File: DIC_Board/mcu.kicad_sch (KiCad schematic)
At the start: 67 parts, among them J1 DM3AT-SF-PEJM5, J2 Conn_ARM_JTAG_SWD_10, P1 USB_C_Plug_USB2.0, SW1 SW_Push, U1 STM32L476ZGTx, U2 AB-RTCMC-32.768kHz-EOA9-S3, U3 APS6404L-3SQRX-SN, Y1 ABM8AAIG-8.000MHz-V2R-T3, Y2 ABS06-107-32.768KHZ-T

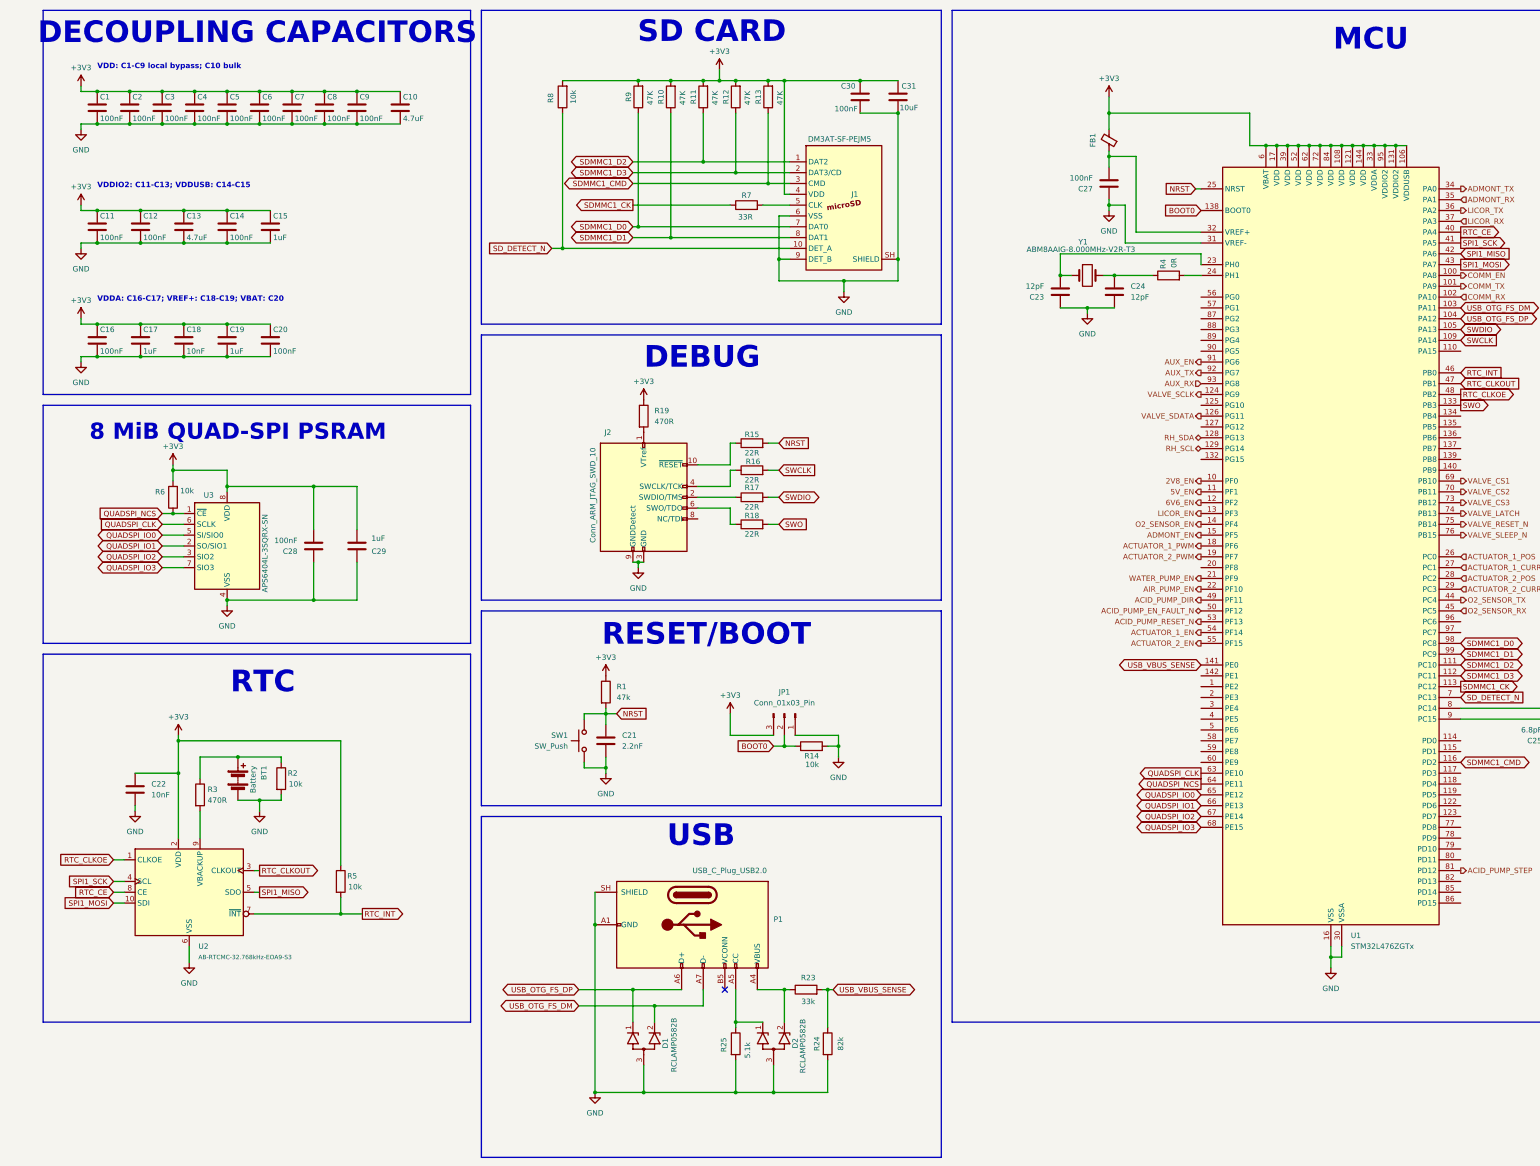
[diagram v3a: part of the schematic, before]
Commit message: Updated board for layout! All footprints added
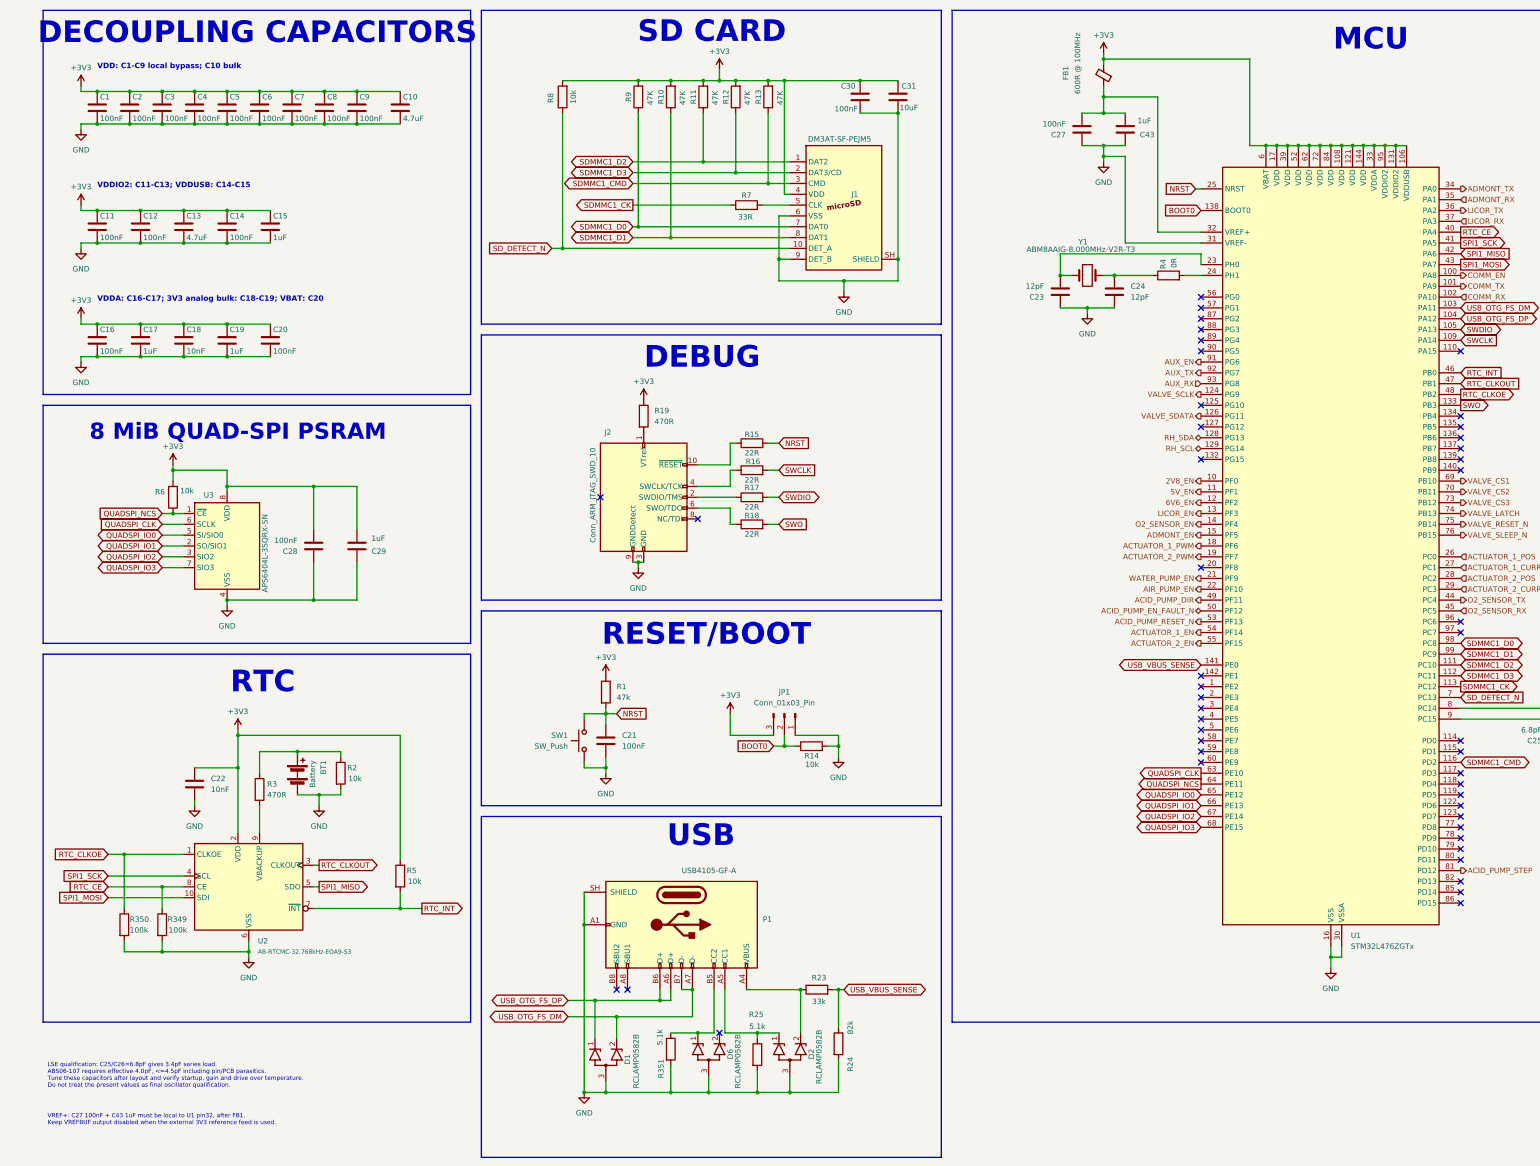
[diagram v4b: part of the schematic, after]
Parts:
- added C43: 1uF, Capacitor_SMD:C_0603_1608Metric, symbol Device:C
- added D6: RCLAMP0582B, Package_TO_SOT_SMD:SOT-523, symbol DIC_Board:RCLAMP0582B_ReviewFixed
- added R349, R350: 100k, Resistor_SMD:R_0603_1608Metric, symbol Device:R
- added R351: 5.1k, Resistor_SMD:R_0402_1005Metric, symbol Device:R
- BT1: footprint (none) -> DIC_Board:BatteryHolder_Keystone_3013_1x16mm; BOM Comments (none) -> 16mm coin-cell retainer only; battery purchased separately.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; BOM Source (none) -> https://www.digikey.com/en/products/detail/keystone-electro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; DigiKey (none) -> 36-3013-ND; MPN (none) -> 3013; Manufacturer (none) -> Keystone Electronics
- C1, C11, C12, C14, C16, C2, C20, C28, C3, C30, C4, C5, C6, C7, C8, C9: BOM Source (none) -> https://product.tdk.com/en/search/capacitor/ceramic/mlcc/in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; Dielectric (none) -> X7R; MPN (none) -> C1608X7R1H104K080AA; Manufacturer (none) -> TDK; Tolerance (none) -> 10%; Voltage Rating (none) -> 50V
- C10, C13: BOM Source (none) -> https://product.tdk.com/en/search/capacitor/ceramic/mlcc/in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; Dielectric (none) -> X7R; MPN (none) -> C2012X7R1E475K125AB; Manufacturer (none) -> TDK; Tolerance (none) -> 10%; Voltage Rating (none) -> 25V
- C15, C17, C19, C29: BOM Source (none) -> https://product.tdk.com/en/search/capacitor/ceramic/mlcc/in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; Dielectric (none) -> X7R; MPN (none) -> C1608X7R1E105K080AB; Manufacturer (none) -> TDK; Tolerance (none) -> 10%; Voltage Rating (none) -> 25V
- C18: BOM Source (none) -> https://product.tdk.com/en/search/capacitor/ceramic/mlcc/in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; Dielectric (none) -> X7R; MPN (none) -> C1608X7R1H103K080AA; Manufacturer (none) -> TDK; Tolerance (none) -> 10%; Voltage Rating (none) -> 50V
- C21: value 2.2nF -> 100nF; footprint (none) -> Capacitor_SMD:C_0603_1608Metric; BOM Source (none) -> https://product.tdk.com/en/search/capacitor/ceramic/mlcc/in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; Dielectric (none) -> X7R; MPN (none) -> C1608X7R1H104K080AA; Manufacturer (none) -> TDK; Tolerance (none) -> 10%; Voltage Rating (none) -> 50V
- C22: footprint (none) -> Capacitor_SMD:C_0603_1608Metric; BOM Source (none) -> https://product.tdk.com/en/search/capacitor/ceramic/mlcc/in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; Dielectric (none) -> X7R; MPN (none) -> C1608X7R1H103K080AA; Manufacturer (none) -> TDK; Tolerance (none) -> 10%; Voltage Rating (none) -> 50V
- C23, C24: footprint (none) -> Capacitor_SMD:C_0603_1608Metric; BOM Source (none) -> https://product.tdk.com/en/search/capacitor/ceramic/mlcc/in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; Dielectric (none) -> C0G; MPN (none) -> C1608C0G1H120J080AA; Manufacturer (none) -> TDK; Tolerance (none) -> 5%; Voltage Rating (none) -> 50V
- C25, C26: footprint (none) -> Capacitor_SMD:C_0402_1005Metric; BOM Source (none) -> https://www.ti.com/lit/df/tidrgo6/tidrgo6.pdf; Dielectric (none) -> C0G; MPN (none) -> GRM1555C1H6R8CA01D; Manufacturer (none) -> Murata; Tolerance (none) -> 0.25pF; Voltage Rating (none) -> 50V
- C27: footprint (none) -> Capacitor_SMD:C_0603_1608Metric; BOM Source (none) -> https://product.tdk.com/en/search/capacitor/ceramic/mlcc/in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; Dielectric (none) -> X7R; MPN (none) -> C1608X7R1H104K080AA; Manufacturer (none) -> TDK; Tolerance (none) -> 10%; Voltage Rating (none) -> 50V
- C31: BOM Source (none) -> https://product.tdk.com/en/search/capacitor/ceramic/mlcc/in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; Dielectric (none) -> X7S; MPN (none) -> C2012X7S1C106K125AC; Manufacturer (none) -> TDK; Tolerance (none) -> 10%; Voltage Rating (none) -> 16V
- D1, D2: symbol Power_Protection:RCLAMP0582B -> DIC_Board:RCLAMP0582B_ReviewFixed
- FB1: value (none) -> 600R @ 100MHz; footprint (none) -> Inductor_SMD:L_0603_1608Metric; BOM Source (none) -> https://www.murata.com/en-us/api/pdfdownloadapi?cate=cgsubC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; Current Rating (none) -> 500mA; DCR Max (none) -> 0.38R; MPN (none) -> BLM18AG601SN1D; Manufacturer (none) -> Murata
- J1: symbol Connector:Micro_SD_Card_Det_Hirose_DM3AT -> DIC_Board:DM3AT_SF_PEJM5_ReviewFixed
- J2: footprint (none) -> DIC_Board:Wurth_61201021621_2x05_P2.54mm_Vertical; BOM Comments (none) -> User-selected 2.54mm-pitch shrouded 10-pin header; retains 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; BOM Source (none) -> https://www.digikey.com/en/products/detail/w%C3%BCrth-elekt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; DigiKey (none) -> 732-2094-ND; MPN (none) -> 61201021621; Manufacturer (none) -> Wurth Elektronik
- JP1: footprint (none) -> DIC_Board:PinHeader_Wurth_61300311121_1x03_P2.54mm_Vertical; BOM Comments (none) -> User specified PTH male header; selected 1x3,2.54mm pitch,v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; BOM Source (none) -> https://www.we-online.com/components/products/datasheet/613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; MPN (none) -> 61300311121; Manufacturer (none) -> Wurth Elektronik
- P1: value USB_C_Plug_USB2.0 -> USB4105-GF-A; footprint (none) -> Connector_USB:USB_C_Receptacle_GCT_USB4105-xx-A_16P_TopMnt_Horizontal; symbol Connector:USB_C_Plug_USB2.0 -> Connector:USB_C_Receptacle_USB2.0_16P; BOM Comments (none) -> Device/UFP socket: CC1 and CC2 each have an independent5.1k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; BOM Source (none) -> https://www.digikey.com/en/products/detail/gct/USB4105-GF-A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; DigiKey (none) -> 2073-USB4105-GF-ACT-ND; MPN (none) -> USB4105-GF-A; Manufacturer (none) -> GCT
- R1: footprint (none) -> Resistor_SMD:R_0603_1608Metric; BOM Source (none) -> https://www.vishay.com/docs/20035/dcrcwe3.pdf; MPN (none) -> CRCW060347K0FKEA; Manufacturer (none) -> Vishay; Power Rating (none) -> 0.125W; Tolerance (none) -> 1%
- R10, R11, R12, R13, R9: BOM Source (none) -> https://www.vishay.com/docs/20035/dcrcwe3.pdf; MPN (none) -> CRCW060347K0FKEA; Manufacturer (none) -> Vishay; Power Rating (none) -> 0.125W; Tolerance (none) -> 1%
- R14, R2, R5: footprint (none) -> Resistor_SMD:R_0603_1608Metric; BOM Source (none) -> https://www.vishay.com/docs/20035/dcrcwe3.pdf; MPN (none) -> CRCW060310K0FKEA; Manufacturer (none) -> Vishay; Power Rating (none) -> 0.125W; Tolerance (none) -> 1%
- R15, R16, R17, R18: footprint (none) -> Resistor_SMD:R_0603_1608Metric; BOM Source (none) -> https://www.vishay.com/docs/20035/dcrcwe3.pdf; MPN (none) -> CRCW060322R0FKEA; Manufacturer (none) -> Vishay; Power Rating (none) -> 0.125W; Tolerance (none) -> 1%
- R19, R3: footprint (none) -> Resistor_SMD:R_0603_1608Metric; BOM Source (none) -> https://www.vishay.com/docs/20035/dcrcwe3.pdf; MPN (none) -> CRCW0603470RFKEA; Manufacturer (none) -> Vishay; Power Rating (none) -> 0.125W; Tolerance (none) -> 1%
- R23: BOM Source (none) -> https://www.vishay.com/docs/20035/dcrcwe3.pdf; MPN (none) -> CRCW040233K0FKED; Manufacturer (none) -> Vishay; Power Rating (none) -> 0.1W; Tolerance (none) -> 1%
- R24: BOM Source (none) -> https://www.vishay.com/docs/20035/dcrcwe3.pdf; MPN (none) -> CRCW040282K0FKED; Manufacturer (none) -> Vishay; Power Rating (none) -> 0.1W; Tolerance (none) -> 1%
- R25: BOM Source (none) -> https://www.vishay.com/docs/20035/dcrcwe3.pdf; MPN (none) -> CRCW04025K10FKED; Manufacturer (none) -> Vishay; Power Rating (none) -> 0.1W; Tolerance (none) -> 1%
- R4: footprint (none) -> Resistor_SMD:R_0603_1608Metric; BOM Source (none) -> https://www.vishay.com/docs/20035/dcrcwe3.pdf; MPN (none) -> CRCW06030000Z0EA; Manufacturer (none) -> Vishay; Power Rating (none) -> 0.125W; Tolerance (none) -> Jumper
- R6, R8: BOM Source (none) -> https://www.vishay.com/docs/20035/dcrcwe3.pdf; MPN (none) -> CRCW060310K0FKEA; Manufacturer (none) -> Vishay; Power Rating (none) -> 0.125W; Tolerance (none) -> 1%
- R7: BOM Source (none) -> https://www.vishay.com/docs/20035/dcrcwe3.pdf; MPN (none) -> CRCW060333R0FKEA; Manufacturer (none) -> Vishay; Power Rating (none) -> 0.125W; Tolerance (none) -> 1%
- SW1: footprint (none) -> DIC_Board:SW_ESwitch_TL6330AF200Q; BOM Comments (none) -> Physical switch terminals 1/2 are internally common and map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; BOM Source (none) -> https://www.e-switch.com/product/tl6330-series-sealed-smt-t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; MPN (none) -> TL6330AF200Q; Manufacturer (none) -> E-Switch
- U1: BOM Source (none) -> https://www.st.com/resource/en/datasheet/stm32l476zg.pdf; MPN (none) -> STM32L476ZGT6; Manufacturer (none) -> STMicroelectronics
- U2: footprint (none) -> Package_SON:RTC_SMD_MicroCrystal_C3_2.5x3.7mm
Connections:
- net GND: now also C43.2, D6.3 (A), R349.2, R350.2, R351.2
- net RTC_CE: now also R349.1
- net RTC_CLKOE: now also R350.1
- net USB_OTG_FS_DM: now also P1.B7 (D-)
- net USB_OTG_FS_DP: now also P1.B6 (D+)
- net at C27.1, FB1.1, U1.32 (VREF+): now also C43.1
- net at P1.B5 (CC2): now also D6.1 (K1), R351.1
- no-connect marks 1 -> 47
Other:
- note added: "LSE qualification: C25/C26=6.8pF gives 3.4pF series load. ABS06-107 requires effective 4.0pF, <=4.5pF including pin/PCB parasitics. Tune these capacitors after layout and verify startup, gain and drive over temperature. Do not treat the present values as final oscillator qualification."
- note added: "VDDA: C16-C17; 3V3 analog bulk: C18-C19; VBAT: C20"
- note added: "VREF+: C27 100nF + C43 1uF must be local to U1 pin32, after FB1. Keep VREFBUF output disabled when the external 3V3 reference feed is used."
- note removed: "VDDA: C16-C17; VREF+: C18-C19; VBAT: C20"
- moved on the sheet: BT1, C22, C27, D1, D2, FB1, R2, R23, R24, R25, R3, R5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

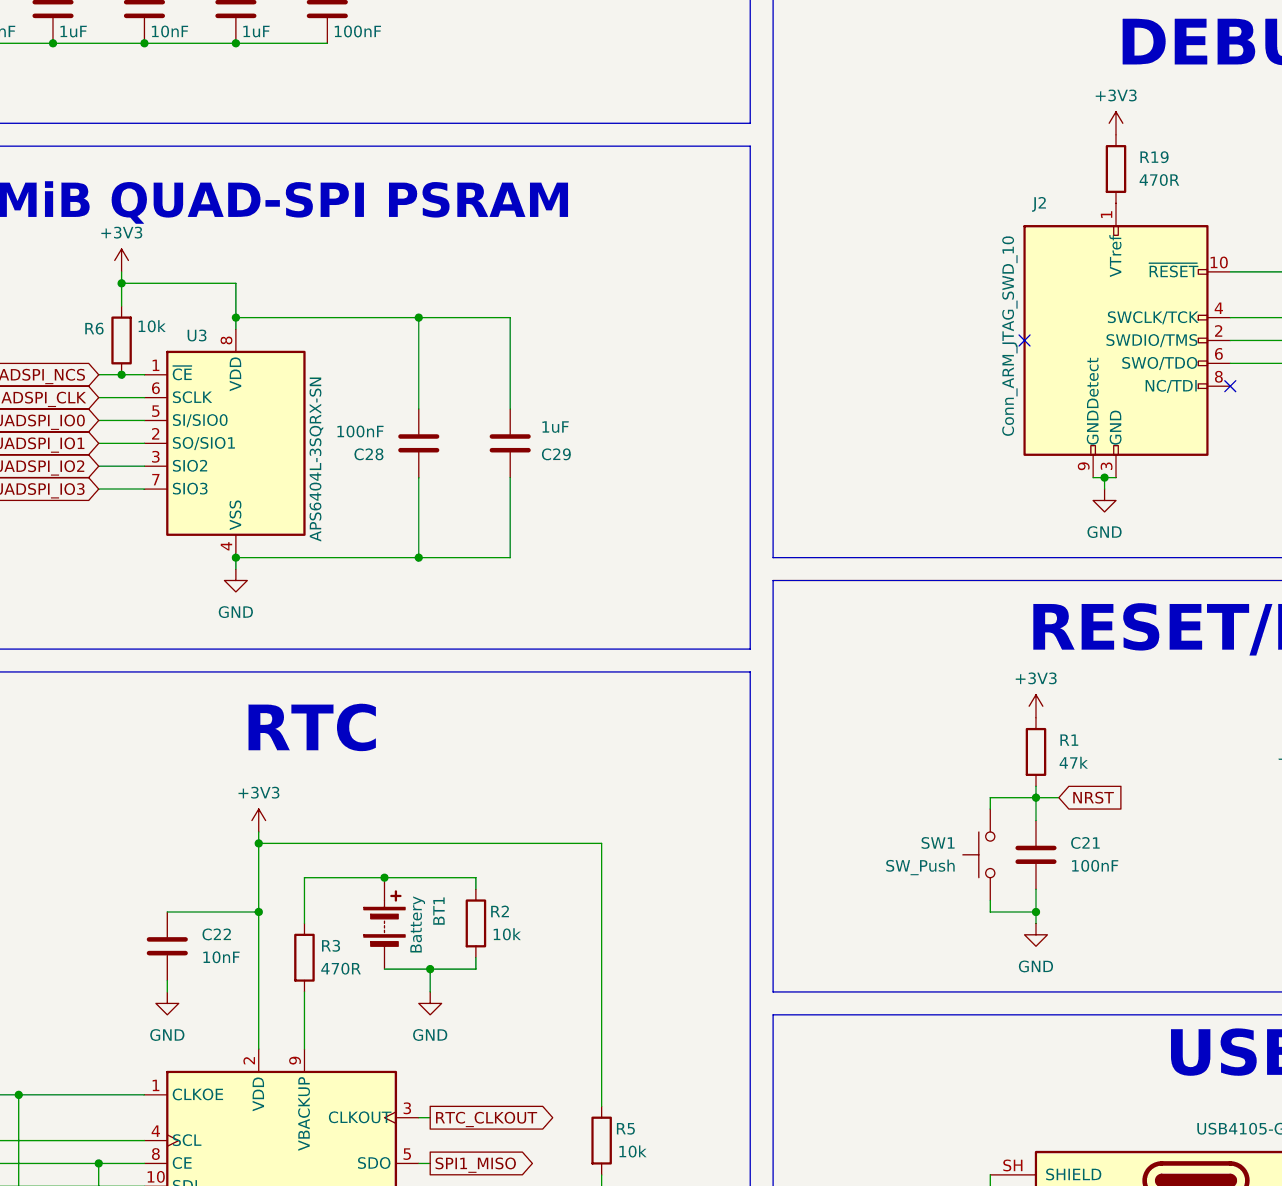
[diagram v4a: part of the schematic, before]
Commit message: Changed the 12V regulator to an integrated IC
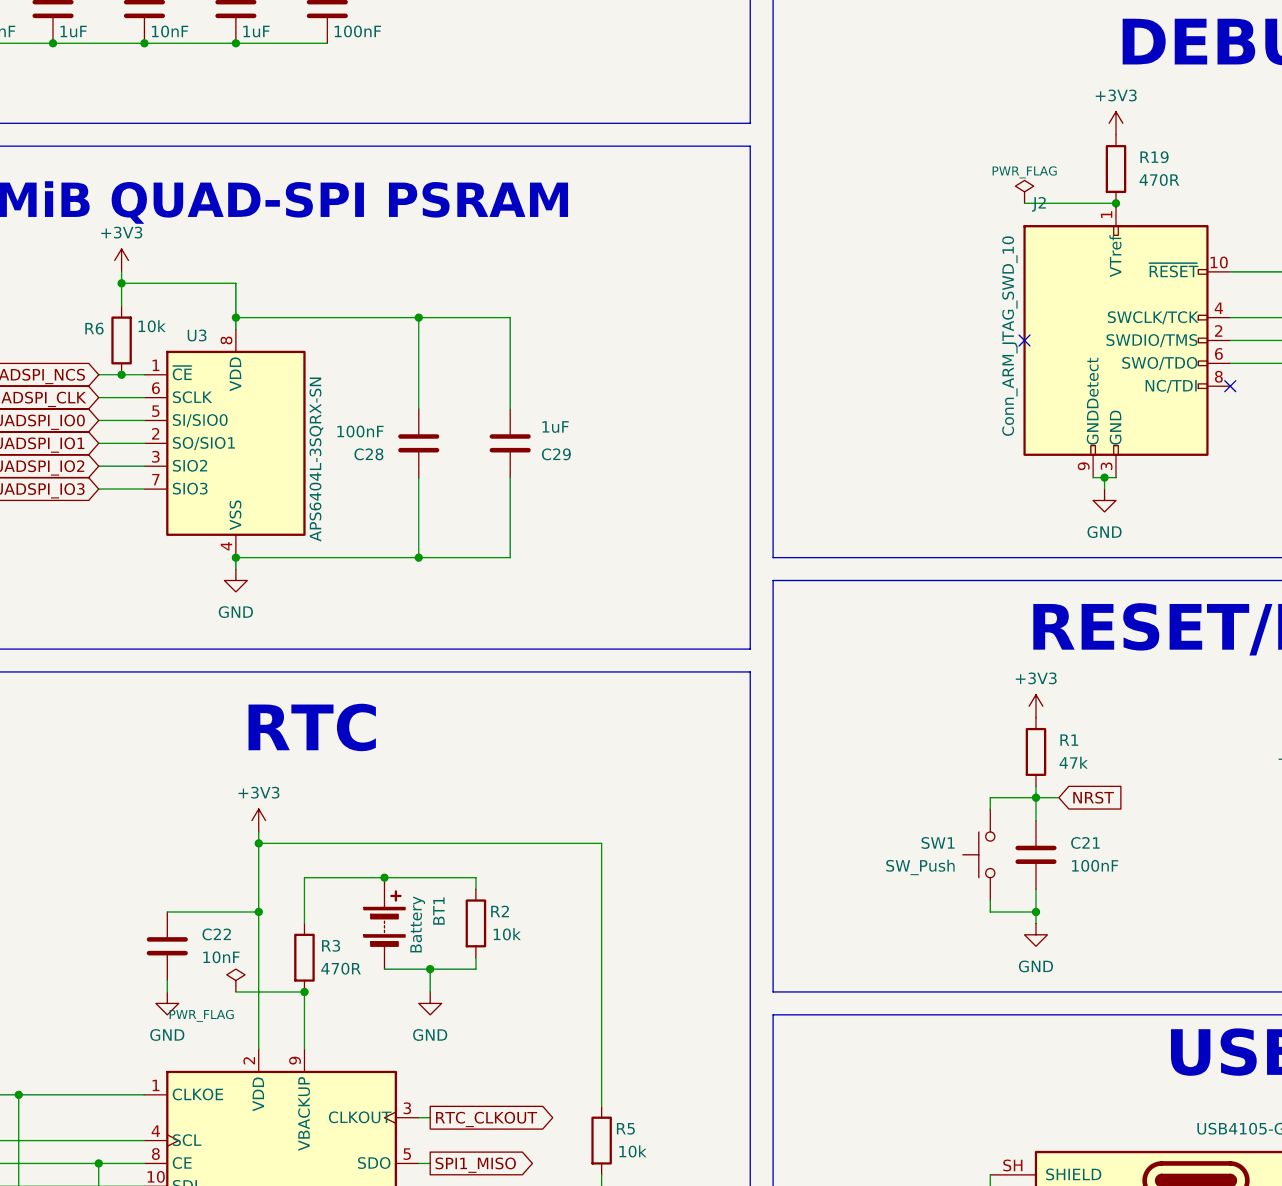
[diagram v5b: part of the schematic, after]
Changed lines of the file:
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@@
 		)
 	)
+ (symbol (lib_id "power:PWR_FLAG") (at 57.15 200.66 0) (unit 1)
+ (exclude_from_sim no) (in_bom no) (on_board yes) (dnp no)
+ (property "Reference" "#FLG0991" (at 57.15 198.755 0) (effects (font (size 1.27 1.27)) (hide yes)))
+ (property "Value" "PWR_FLAG" (at 53.34 203.2 0) (effects (font (size 1 1))))
+ (property "Footprint" "" (at 57.15 200.66 0) (effects (font (size 1.27 1.27)) (hide yes)))
+ (property "Datasheet" "" (at 57.15 200.66 0) (effects (font (size 1.27 1.27)) (hide yes)))
+ (pin "1")
+ (instances (project "DIC_Board" (path "/bb0ef0df-c181-443a-843c-695cd2e0efee/ef2b3969-ba29-4866-a95a-5e275b2bf226" (reference "#FLG0991") (unit 1)))))
+ (wire (pts (xy 57.15 200.66) (xy 64.77 200.66)) (stroke (width 0) (type default)))
+ (junction (at 64.77 200.66) (diameter 0) (color 0 0 0 0))
+ (symbol (lib_id "power:PWR_FLAG") (at 144.78 113.03 0) (unit 1)
+ (exclude_from_sim no) (in_bom no) (on_board yes) (dnp no)
+ (property "Reference" "#FLG0992" (at 144.78 111.125 0) (effects (font (size 1.27 1.27)) (hide yes)))
+ (property "Value" "PWR_FLAG" (at 144.78 109.474 0) (effects (font (size 1 1))))
+ (property "Footprint" "" (at 144.78 113.03 0) (effects (font (size 1.27 1.27)) (hide yes)))
+ (property "Datasheet" "" (at 144.78 113.03 0) (effects (font (size 1.27 1.27)) (hide yes)))
+ (pin "1")
+ (instances (project "DIC_Board" (path "/bb0ef0df-c181-443a-843c-695cd2e0efee/ef2b3969-ba29-4866-a95a-5e275b2bf226" (reference "#FLG0992") (unit 1)))))
+ (wire (pts (xy 144.78 113.03) (xy 154.94 113.03)) (stroke (width 0) (type default)))
+ (junction (at 154.94 113.03) (diameter 0) (color 0 0 0 0))
 )
